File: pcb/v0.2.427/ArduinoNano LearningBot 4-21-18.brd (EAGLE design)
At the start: 106.9 x 55.1 mm, 19 parts

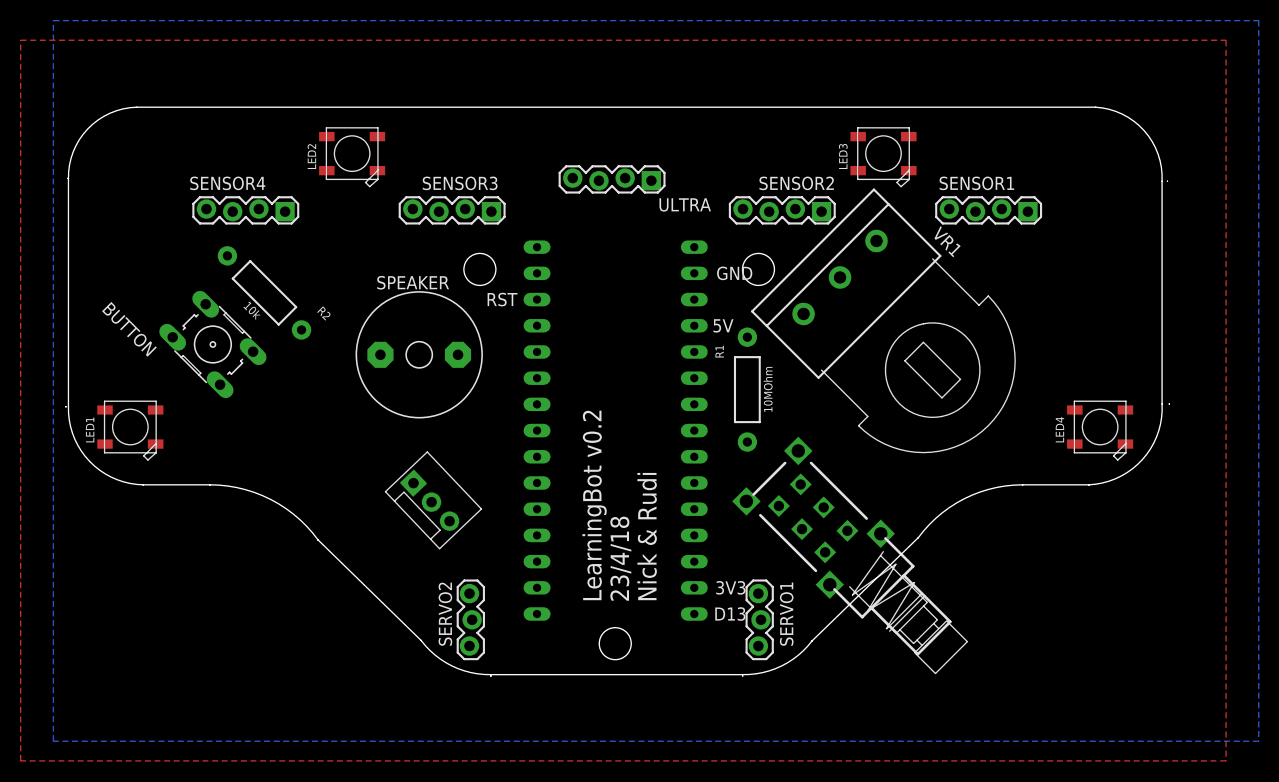
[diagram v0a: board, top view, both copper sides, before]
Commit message: changed designators and holes
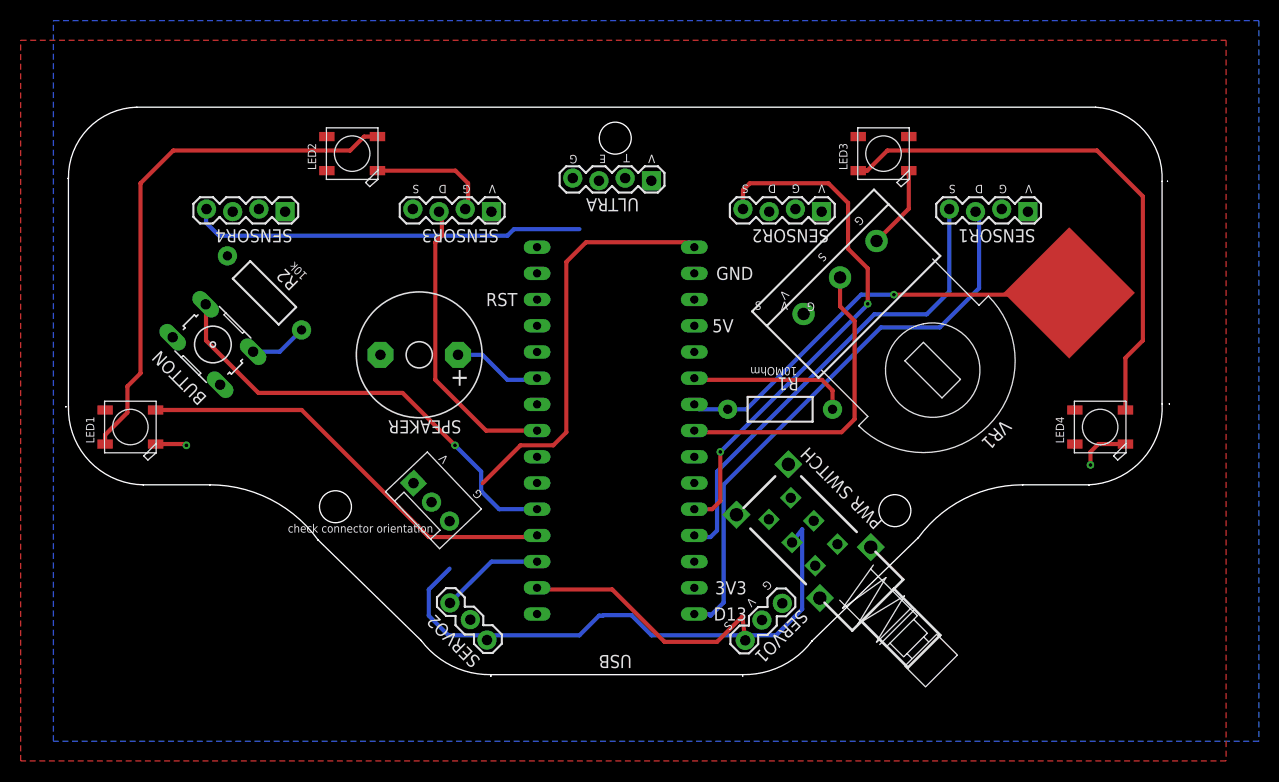
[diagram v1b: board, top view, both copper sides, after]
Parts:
- added TOUCH: TOUCHSENSOR, CapTouch:TOUCH1
- moved SERVO1 4.72 mm to (69.1, 7.00), turned to 225 degrees
- moved R1 3.70 mm to (69.0, 25.7), turned to 180 degrees
- moved SERVO2 1.79 mm to (40.7, 3.44), turned to 135 degrees
- moved S1 1.62 mm to (71.0, 13.7)
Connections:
- removed net LED-1: LED1.4-DIN
- removed net N.C.: S1.NO1, U$1.GND
- new net GND: LED1.3-GND, LED2.3-GND, LED3.3-GND, LED4.3-GND, R2.P$2, SENSOR1.2, SENSOR2.2, SENSOR3.2, SENSOR4.2, SERVO1.1, SERVO2.1, SPEAKER.1, U$1.GND, U$1.GND1, ULTRA.4, VR1.1
- net GND-ISO: now also BAT.3; no longer LED1.3-GND, LED2.3-GND, LED3.3-GND, LED4.3-GND, R2.P$2, SENSOR1.2, SENSOR2.2, SENSOR3.2, SENSOR4.2, SERVO1.1, SERVO2.1, SPEAKER.1, U$1.GND1, ULTRA.4, VR1.1
- net LEDS: now also LED1.4-DIN
- net N$9: now also BAT.1; no longer BAT.3
- net RAWIN: now also S1.NO1; no longer BAT.1
- net TOUCH: now also TOUCH.P$1
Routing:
- net LDR1_DO: track 0.00 -> 55.1 mm
- net N$9: track 0.00 -> 54.4 mm
- net N$4: track 0.00 -> 51.6 mm
- net N$5: track 0.00 -> 51.5 mm
- net SENSOR2: track 0.00 -> 51.5 mm, vias 0 -> 2
- net SENSOR1: track 0.00 -> 46.0 mm
- net BUTTON: track 0.00 -> 43.5 mm, vias 0 -> 1
- net LEDS: track 0.00 -> 42.1 mm
- net TOUCH: track 0.00 -> 41.2 mm, vias 0 -> 1
- net RAWIN: track 0.00 -> 40.1 mm
- net SENSOR4: track 0.00 -> 38.3 mm
- net POTPIN: track 0.00 -> 30.4 mm
- net IR_SENSOR2_DO: track 0.00 -> 28.6 mm
- net GND: track 0.00 -> 28.0 mm, vias 0 -> 2
- net N$6: track 0.00 -> 25.4 mm
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- added copper zone on layer 16, net GND
- removed copper zone on layer 16, net N.C.
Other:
- board text added: "+"
- board text added: "D"
- board text added: "E"
- board text added: "G"
- board text added: "LearningBot v0.2.18427 KodingKreators Designed by Nick"
- board text added: "PWR SWITCH"
- board text added: "S"
- board text added: "T"
- board text added: "USB"
- board text added: "V"
- board text added: "check connector orientation"
- board text removed: "LearningBot v0.2 23/4/18 Nick & Rudi"

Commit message: most recent board
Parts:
- moved R1 6.99 mm to (64.5, 31.1), turned to 270 degrees
- moved ULTRA 0.32 mm to (56.5, 47.7)
- turned SPEAKER to 270 degrees
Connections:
- removed net GND-ISO: BAT.3
- removed net N$2: LED3.4-DIN
- net GND: now also BAT.3
- net N$1: now also LED3.4-DIN
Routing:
- net N$1: track 0.00 -> 64.3 mm, vias 0 -> 2
- net IR_SENSOR1_DO: track 0.00 -> 58.6 mm, vias 0 -> 2
- net SENSOR3: track 0.00 -> 52.3 mm, vias 0 -> 1
- net GND: track 28.0 -> 76.1 mm, vias 2 -> 5
- net LDR2_DO: track 0.00 -> 45.7 mm, vias 0 -> 2
- net TRIG_PIN: track 0.00 -> 37.5 mm, vias 0 -> 1
- net SENSOR4: track 38.3 -> 74.6 mm, vias 0 -> 3
- net ECHO_PIN: track 0.00 -> 32.5 mm, vias 0 -> 1
- net VCC: track 0.00 -> 31.7 mm
- net SENSOR2: track 51.5 -> 39.2 mm, vias 2 -> 1
- net SENSOR1: track 46.0 -> 53.6 mm, vias 0 -> 1
- net N$5: track 51.5 -> 58.8 mm
- net RAWIN: track 40.1 -> 32.9 mm, vias 0 -> 2
- net LEDS: track 42.1 -> 47.8 mm
- net N$6: track 25.4 -> 30.7 mm
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
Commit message: with gerbers
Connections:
- net VCC: no longer BUTTON.3
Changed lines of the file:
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@@
 <contactref element="VR1" pad="3"/>
 <contactref element="U$1" pad="5V"/>
-<contactref element="BUTTON" pad="3"/>
 <contactref element="SERVO1" pad="2"/>
 <contactref element="SERVO2" pad="2"/>
@@
 </signal>
 <signal name="TOUCH">
-<contactref element="U$1" pad="A5"/>
 <contactref element="R1" pad="P$2"/>
 <contactref element="TOUCH" pad="P$1"/>
-<wire x1="60.66" y1="26.194" x2="63.426" y2="26.194" width="0.4064" layer="16"/>
-<wire x1="63.426" y1="26.194" x2="64.535" y2="26.0375" width="0.4064" layer="16"/>
 <wire x1="96.83" y1="36.83" x2="97" y2="37" width="0.4064" layer="1"/>
 <wire x1="96.83" y1="36.83" x2="67.945" y2="36.83" width="0.4064" layer="1"/>
-<wire x1="65.405" y1="26.9075" x2="64.535" y2="26.0375" width="0.4064" layer="1"/>
+<wire x1="64.535" y1="26.0375" x2="65.405" y2="26.9075" width="0.4064" layer="1"/>
 <wire x1="67.945" y1="36.83" x2="65.405" y2="34.29" width="0.4064" layer="1"/>
 <wire x1="65.405" y1="34.29" x2="65.405" y2="26.9075" width="0.4064" layer="1"/>
+<contactref element="U$1" pad="A5"/>
+<wire x1="64.3785" y1="26.194" x2="64.535" y2="26.0375" width="0.4064" layer="1"/>
+<wire x1="60.66" y1="26.194" x2="64.3785" y2="26.194" width="0.4064" layer="1"/>
+<wire x1="64.3785" y1="26.194" x2="64.535" y2="26.0375" width="0.4064" layer="1"/>
 </signal>
 <signal name="CAP_TOUCH_RECEIVE_PIN">

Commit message: Hopefully, the last one
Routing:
- net RAWIN: track 32.9 -> 31.9 mm
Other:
- board text removed: "check connector orientation"
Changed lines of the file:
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@@
 <text x="40.2082" y="17.5006" size="0.8128" layer="25" rot="SR135">G</text>
 <text x="36.8808" y="20.955" size="0.8128" layer="25" rot="SR135">V</text>
-<text x="21.2598" y="13.7668" size="0.8128" layer="25">check connector orientation</text>
 <text x="38.9636" y="47.4726" size="0.8128" layer="25" rot="SR180">G</text>
 <text x="41.4274" y="47.4726" size="0.8128" layer="25" rot="SR180">V</text>
@@
 <contactref element="U$1" pad="RAW"/>
 <contactref element="S1" pad="NO1"/>
-<wire x1="60.66" y1="41.434" x2="66.516" y2="41.434" width="0.4064" layer="1"/>
-<wire x1="66.516" y1="41.434" x2="67.945" y2="40.005" width="0.4064" layer="1"/>
-<via x="67.945" y="17.4625" extent="1-16" drill="0.35" shape="square"/>
-<wire x1="67.945" y1="17.4625" x2="67.945" y2="15.104928125" width="0.4064" layer="1"/>
-<wire x1="67.945" y1="15.104928125" x2="67.891709375" y2="15.0516375" width="0.4064" layer="1"/>
-<wire x1="67.945" y1="40.005" x2="67.945" y2="17.4625" width="0.4064" layer="16"/>
-<via x="67.945" y="40.005" extent="1-16" drill="0.35" shape="square"/>
+<wire x1="60.66" y1="41.434" x2="64.135" y2="41.434" width="0.4064" layer="1"/>
+<wire x1="67.891709375" y1="15.0516375" x2="66.675" y2="16.268346875" width="0.4064" layer="1"/>
+<via x="66.675" y="21.9075" extent="1-16" drill="0.35" shape="square"/>
+<wire x1="66.675" y1="21.9075" x2="66.675" y2="39.6875" width="0.4064" layer="16"/>
+<wire x1="64.9285" y1="41.434" x2="64.135" y2="41.434" width="0.4064" layer="16"/>
+<via x="64.135" y="41.434" extent="1-16" drill="0.35" shape="square"/>
+<wire x1="66.675" y1="16.268346875" x2="66.675" y2="21.9075" width="0.4064" layer="1"/>
+<wire x1="66.675" y1="39.6875" x2="64.9285" y2="41.434" width="0.4064" layer="16"/>
 </signal>
 <signal name="BUTTON">
